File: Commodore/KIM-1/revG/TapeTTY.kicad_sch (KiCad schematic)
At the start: 45 parts

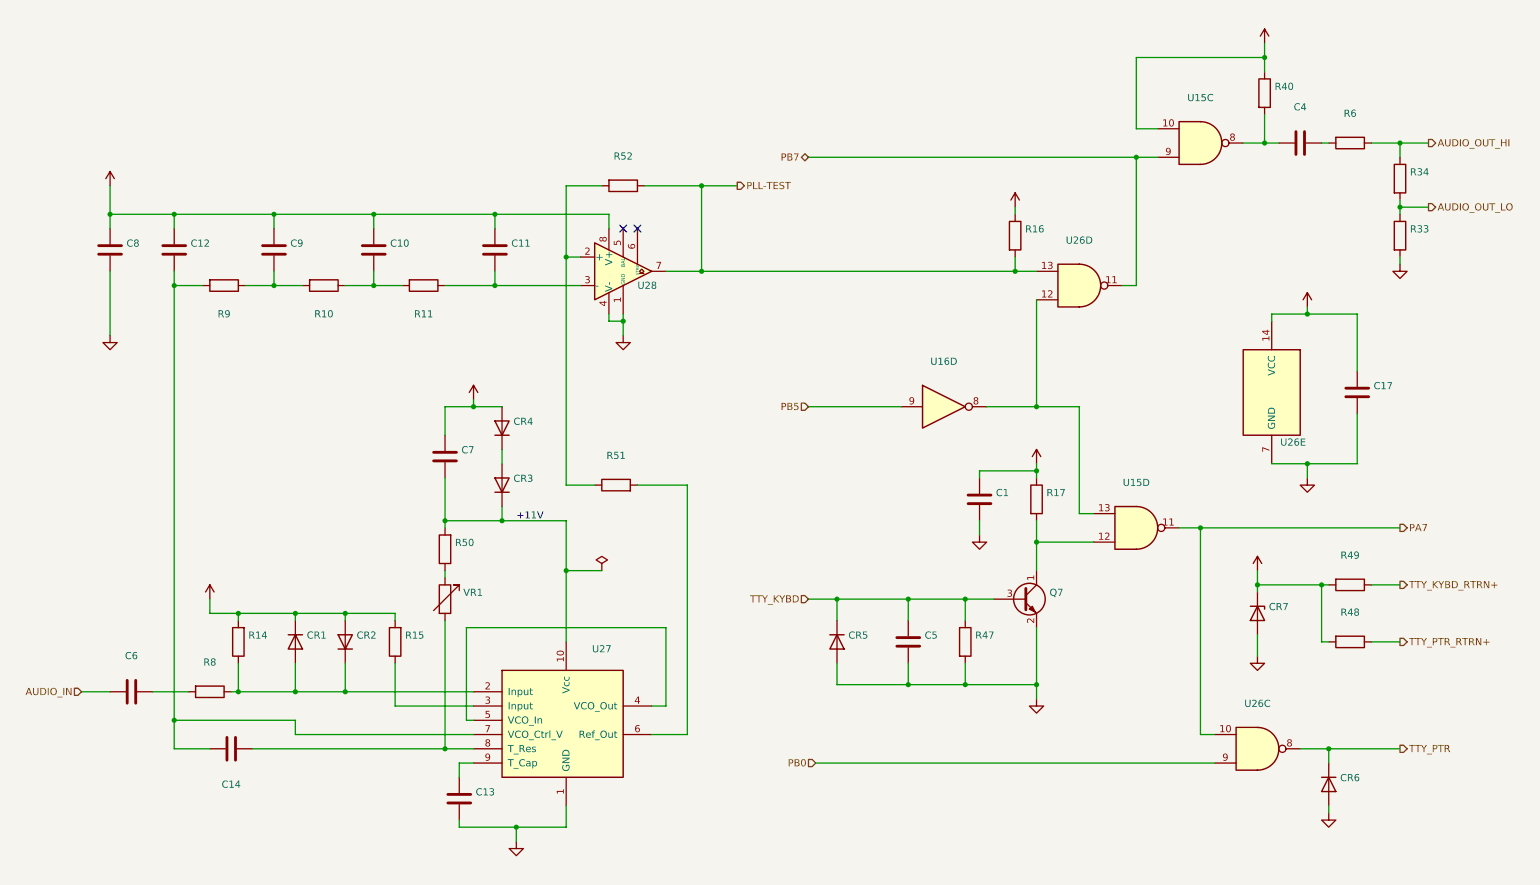
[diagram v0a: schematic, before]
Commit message: Corrected resistor values for R18..R23 and R41..R46 (transposed).
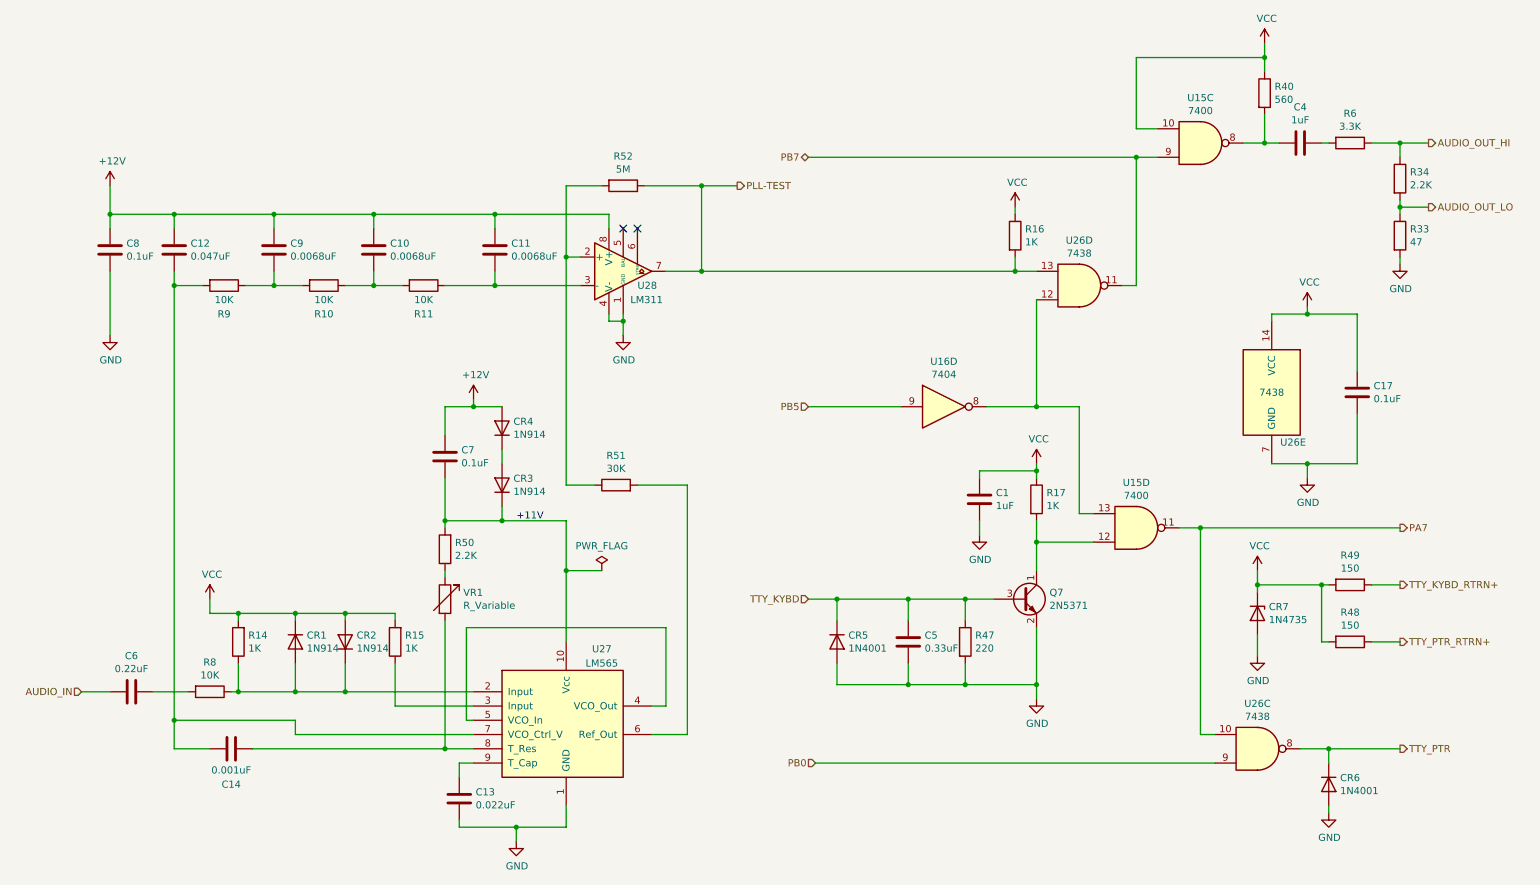
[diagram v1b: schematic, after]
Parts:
- C1, C4: value (none) -> 1uF
- C10, C11, C9: value (none) -> 0.0068uF
- C12: value (none) -> 0.047uF
- C13: value (none) -> 0.022uF
- C14: value (none) -> 0.001uF
- C17, C7, C8: value (none) -> 0.1uF
- C5: value (none) -> 0.33uF
- C6: value (none) -> 0.22uF
- CR1, CR2, CR3, CR4: value (none) -> 1N914
- CR5, CR6: value (none) -> 1N4001
- CR7: value (none) -> 1N4735
- Q7: value (none) -> 2N5371
- R10, R11, R8, R9: value (none) -> 10K
- R14, R15, R16, R17: value (none) -> 1K
- R33: value (none) -> 47
- R34, R50: value (none) -> 2.2K
- R40: value (none) -> 560
- R47: value (none) -> 220
- R48, R49: value (none) -> 150
- R51: value (none) -> 30K
- R52: value (none) -> 5M
- R6: value (none) -> 3.3K
- U15: value (none) -> 7400
- U16: value (none) -> 7404
- U26: value (none) -> 7438
- U27: value (none) -> LM565
- U28: value (none) -> LM311
- VR1: value (none) -> R_Variable
